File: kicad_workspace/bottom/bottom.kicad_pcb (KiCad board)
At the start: 2 copper layers, 76.8 x 84 mm, 28 parts, among them M1 N20_MOTOR_EXTENDED_SHAFT, M2 N20_MOTOR_EXTENDED_SHAFT, U1 DRV8833PWP, U2 ULTRASOUND_T_R, U3 ATmega4809-A, U4 BNO055, Y1 32.768kHz

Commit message: add battery connector
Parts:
- added J1: Battery connector, Connector_JST:JST_XH_B2B-XH-AM_1x02_P2.50mm_Vertical, F.Cu at (75.2, 89.9)
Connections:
- U1 pad 10: Net-(U1-BIN2) -> DRV_B2
- U1 pad 15: Net-(U1-AIN2) -> DRV_A2
- U1 pad 16: Net-(U1-AIN1) -> DRV_A1
- U1 pad 9: Net-(U1-BIN1) -> DRV_B1
- U3 pad 34: Net-(U1-BIN2) -> DRV_A1
- U3 pad 35: Net-(U1-BIN1) -> DRV_A2
- U3 pad 36: Net-(U1-AIN2) -> DRV_B1
- U3 pad 37: Net-(U1-AIN1) -> DRV_B2
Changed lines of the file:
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@@
   (net 13 "Net-(U1-BISEN)")
   (net 14 "unconnected-(U1-nFAULT-Pad8)")
-  (net 15 "Net-(U1-BIN1)")
-  (net 16 "Net-(U1-BIN2)")
+  (net 15 "VCC")
+  (net 16 "DRV_B1")
   (net 17 "Net-(U1-VCP)")
-  (net 18 "Net-(U1-AIN2)")
-  (net 19 "Net-(U1-AIN1)")
+  (net 18 "DRV_B2")
+  (net 19 "DRV_A2")
   (net 20 "Net-(U2-SIG)")
   (net 21 "Net-(JP1-C)")
@@
   (net 73 "unconnected-(U6-GPIO1-Pad5)")
   (net 74 "unconnected-(U7-GPIO1-Pad5)")
+  (net 75 "DRV_A1")
   (footprint "pololu:ULTRASOUND_T_R" (layer "F.Cu")
     (at 60.325 38.1)
@@
       (scale (xyz 1 1 1))
       (rotate (xyz 0 180 180))
+    )
+  )
+  (footprint "Connector_JST:JST_XH_B2B-XH-AM_1x02_P2.50mm_Vertical" (layer "F.Cu")
+    (at 75.224 89.916)
+    (descr "JST XH series connector, B2B-XH-AM, with boss (http://www.jst-mfg.com/product/pdf/eng/eXH.pdf), generated with kicad-footprint-generator")
+    (tags "connector JST XH vertical boss")
+    (property "Sheetfile" "bottom.kicad_sch")
+    (property "Sheetname" "")
+    (property "ki_description" "Generic connector, single row, 01x02, script generated (kicad-library-utils/schlib/autogen/connector/)")
+    (property "ki_keywords" "connector")
+    (attr through_hole)
+    (fp_text reference "J1" (at 1.25 -3.55) (layer "F.SilkS")
+        (effects (font (size 1 1) (thickness 0.15)))
+    )
+    (fp_text value "Battery connector" (at 1.25 4.6) (layer "F.Fab")
+        (effects (font (size 1 1) (thickness 0.15)))
+    )
+    (fp_text user "${REFERENCE}" (at 1.25 2.7) (layer "F.Fab")
+        (effects (font (size 1 1) (thickness 0.15)))
+    )
+    (fp_line (start -2.85 -2.75) (end -2.85 -1.5)
+      (stroke (width 0.12) (type solid)) (layer "F.SilkS"))
+    (fp_line (start -2.56 -2.46) (end -2.56 3.51)
+      (stroke (width 0.12) (type solid)) (layer "F.SilkS"))
+    (fp_line (start -2.56 3.51) (end 5.06 3.51)
+      (stroke (width 0.12) (type solid)) (layer "F.SilkS"))
+    (fp_line (start -2.55 -2.45) (end -2.55 -1.7)
+      (stroke (width 0.12) (type solid)) (layer "F.SilkS"))
+    (fp_line (start -2.55 -1.7) (end -0.75 -1.7)
+      (stroke (width 0.12) (type solid)) (layer "F.SilkS"))
+    (fp_line (start -2.55 -0.2) (end -1.8 -0.2)
+      (stroke (width 0.12) (type solid)) (layer "F.SilkS"))
+    (fp_line (start -1.8 -0.2) (end -1.8 1.14)
+      (stroke (width 0.12) (type solid)) (layer "F.SilkS"))
+    (fp_line (start -1.6 -2.75) (end -2.85 -2.75)
+      (stroke (width 0.12) (type solid)) (layer "F.SilkS"))
+    (fp_line (start -0.75 -2.45) (end -2.55 -2.45)
+      (stroke (width 0.12) (type solid)) (layer "F.SilkS"))
+    (fp_line (start -0.75 -1.7) (end -0.75 -2.45)
+      (stroke (width 0.12) (type solid)) (layer "F.SilkS"))
+    (fp_line (start 0.75 -2.45) (end 0.75 -1.7)
+      (stroke (width 0.12) (type solid)) (layer "F.SilkS"))
+    (fp_line (start 0.75 -1.7) (end 1.75 -1.7)
+      (stroke (width 0.12) (type solid)) (layer "F.SilkS"))
+    (fp_line (start 1.25 2.75) (end -0.74 2.75)
+      (stroke (width 0.12) (type solid)) (layer "F.SilkS"))
+    (fp_line (start 1.75 -2.45) (end 0.75 -2.45)
+      (stroke (width 0.12) (type solid)) (layer "F.SilkS"))
+    (fp_line (start 1.75 -1.7) (end 1.75 -2.45)
+      (stroke (width 0.12) (type solid)) (layer "F.SilkS"))
+    (fp_line (start 3.25 -2.45) (end 3.25 -1.7)
+      (stroke (width 0.12) (type solid)) (layer "F.SilkS"))
+    (fp_line (start 3.25 -1.7) (end 5.05 -1.7)
+      (stroke (width 0.12) (type solid)) (layer "F.SilkS"))
+    (fp_line (start 4.3 -0.2) (end 4.3 2.75)
+      (stroke (width 0.12) (type solid)) (layer "F.SilkS"))
+    (fp_line (start 4.3 2.75) (end 1.25 2.75)
+      (stroke (width 0.12) (type solid)) (layer "F.SilkS"))
+    (fp_line (start 5.05 -2.45) (end 3.25 -2.45)
+      (stroke (width 0.12) (type solid)) (layer "F.SilkS"))
+    (fp_line (start 5.05 -1.7) (end 5.05 -2.45)
+      (stroke (width 0.12) (type solid)) (layer "F.SilkS"))
+    (fp_line (start 5.05 -0.2) (end 4.3 -0.2)
+      (stroke (width 0.12) (type solid)) (layer "F.SilkS"))
+    (fp_line (start 5.06 -2.46) (end -2.56 -2.46)
+      (stroke (width 0.12) (type solid)) (layer "F.SilkS"))
+    (fp_line (start 5.06 3.51) (end 5.06 -2.46)
+      (stroke (width 0.12) (type solid)) (layer "F.SilkS"))
+    (fp_line (start -2.95 -2.85) (end -2.95 3.9)
+      (stroke (width 0.05) (type solid)) (layer "F.CrtYd"))
+    (fp_line (start -2.95 3.9) (end 5.45 3.9)
+      (stroke (width 0.05) (type solid)) (layer "F.CrtYd"))
+    (fp_line (start 5.45 -2.85) (end -2.95 -2.85)
+      (stroke (width 0.05) (type solid)) (layer "F.CrtYd"))
+    (fp_line (start 5.45 3.9) (end 5.45 -2.85)
+      (stroke (width 0.05) (type solid)) (layer "F.CrtYd"))
+    (fp_line (start -2.45 -2.35) (end -2.45 3.4)
+      (stroke (width 0.1) (type solid)) (layer "F.Fab"))
+    (fp_line (start -2.45 3.4) (end 4.95 3.4)
+      (stroke (width 0.1) (type solid)) (layer "F.Fab"))
+    (fp_line (start -0.625 -2.35) (end 0 -1.35)
+      (stroke (width 0.1) (type solid)) (layer "F.Fab"))
+    (fp_line (start 0 -1.35) (end 0.625 -2.35)
+      (stroke (width 0.1) (type solid)) (layer "F.Fab"))
+    (fp_line (start 4.95 -2.35) (end -2.45 -2.35)
+      (stroke (width 0.1) (type solid)) (layer "F.Fab"))
+    (fp_line (start 4.95 3.4) (end 4.95 -2.35)
+      (stroke (width 0.1) (type solid)) (layer "F.Fab"))
+    (pad "" np_thru_hole circle (at -1.6 2) (size 1.2 1.2) (drill 1.2) (layers "*.Cu" "*.Mask"))
+    (pad "1" thru_hole roundrect (at 0 0) (size 1.7 2) (drill 1) (layers "*.Cu" "*.Mask") (roundrect_rratio 0.147059)
+      (net 15 "VCC") (pinfunction "Pin_1") (pintype "passive"))
+    (pad "2" thru_hole oval (at 2.5 0) (size 1.7 2) (drill 1) (layers "*.Cu" "*.Mask")
+      (net 1 "GND") (pinfunction "Pin_2") (pintype "passive"))
+    (model "${KICAD7_3DMODEL_DIR}/Connector_JST.3dshapes/JST_XH_B2B-XH-A_1x02_P2.50mm_Vertical.step"
+      (offset (xyz 0 0 0))
+      (scale (xyz 1 1 1))
+      (rotate (xyz 0 0 0))
     )
   )
@@
     (fp_arc (start -4.277996 -4.277996) (mid -5.350166 -3.264983) (end -6.75 -2.8)
       (stroke (width 0.12) (type solid)) (layer "B.SilkS"))
-    (fp_arc (start 4.277996 4.277996) (mid 5.350166 3.264983) (end 6.75 2.8)
+    (fp_arc (start 4.277996 4.277996) (mid 5.350166 3.264984) (end 6.75 2.8)
       (stroke (width 0.12) (type solid)) (layer "B.SilkS"))
     (fp_arc (start 5.988332 0.861605) (mid 0 6.049999) (end -5.988332 0.861605)
       (stroke (width 0.12) (type solid)) (layer "B.SilkS"))
-    (fp_arc (start 6.75 -2.8) (mid 5.350172 -3.264989) (end 4.277997 -4.277996)
+    (fp_arc (start 6.75 -2.8) (mid 5.350172 -3.264991) (end 4.277997 -4.277996)
       (stroke (width 0.12) (type solid)) (layer "B.SilkS"))
     (fp_arc (start 6.75 -2.8) (mid 9.55 0) (end 6.75 2.8)
@@
       (net 14 "unconnected-(U1-nFAULT-Pad8)") (pinfunction "nFAULT") (pintype "open_collector+no_connect"))
     (pad "9" smd roundrect (at 2.8625 -2.275 180) (size 1.575 0.4) (layers "B.Cu" "B.Paste" "B.Mask") (roundrect_rratio 0.25)
-      (net 15 "Net-(U1-BIN1)") (pinfunction "BIN1") (pintype "input"))
+      (net 16 "DRV_B1") (pinfunction "BIN1") (pintype "input"))
     (pad "10" smd roundrect (at 2.8625 -1.625 180) (size 1.575 0.4) (layers "B.Cu" "B.Paste" "B.Mask") (roundrect_rratio 0.25)
-      (net 16 "Net-(U1-BIN2)") (pinfunction "BIN2") (pintype "input"))
+      (net 18 "DRV_B2") (pinfunction "BIN2") (pintype "input"))
     (pad "11" smd roundrect (at 2.8625 -0.975 180) (size 1.575 0.4) (layers "B.Cu" "B.Paste" "B.Mask") (roundrect_rratio 0.25)
       (net 17 "Net-(U1-VCP)") (pinfunction "VCP") (pintype "bidirectional"))
@@
       (net 22 "+3.3V") (pinfunction "VINT") (pintype "power_in"))
     (pad "15" smd roundrect (at 2.8625 1.625 180) (size 1.575 0.4) (layers "B.Cu" "B.Paste" "B.Mask") (roundrect_rratio 0.25)
-      (net 18 "Net-(U1-AIN2)") (pinfunction "AIN2") (pintype "input"))
+      (net 19 "DRV_A2") (pinfunction "AIN2") (pintype "input"))
     (pad "16" smd roundrect (at 2.8625 2.275 180) (size 1.575 0.4) (layers "B.Cu" "B.Paste" "B.Mask") (roundrect_rratio 0.25)
-      (net 19 "Net-(U1-AIN1)") (pinfunction "AIN1") (pintype "input"))
+      (net 75 "DRV_A1") (pinfunction "AIN1") (pintype "input"))
     (pad "17" thru_hole circle (at -0.75 -1.5 180) (size 0.5 0.5) (drill 0.2) (layers "*.Cu")
       (net 1 "GND") (pinfunction "GND(PPAD)") (pintype "power_in"))
@@
       (net 47 "unconnected-(U3-PE3-Pad33)") (pinfunction "PE3") (pintype "bidirectional+no_connect"))
     (pad "34" smd roundrect (at 4.1625 1.75 180) (size 1.475 0.3) (layers "B.Cu" "B.Paste" "B.Mask") (roundrect_rratio 0.25)
-      (net 16 "Net-(U1-BIN2)") (pinfunction "PF0") (pintype "bidirectional"))
+      (net 75 "DRV_A1") (pinfunction "PF0") (pintype "bidirectional"))
     (pad "35" smd roundrect (at 4.1625 2.25 180) (size 1.475 0.3) (layers "B.Cu" "B.Paste" "B.Mask") (roundrect_rratio 0.25)
-      (net 15 "Net-(U1-BIN1)") (pinfunction "PF1") (pintype "bidirectional"))
+      (net 19 "DRV_A2") (pinfunction "PF1") (pintype "bidirectional"))
     (pad "36" smd roundrect (at 4.1625 2.75 180) (size 1.475 0.3) (layers "B.Cu" "B.Paste" "B.Mask") (roundrect_rratio 0.25)
-      (net 18 "Net-(U1-AIN2)") (pinfunction "PF2") (pintype "bidirectional"))
+      (net 16 "DRV_B1") (pinfunction "PF2") (pintype "bidirectional"))
     (pad "37" smd roundrect (at 2.75 4.1625 180) (size 0.3 1.475) (layers "B.Cu" "B.Paste" "B.Mask") (roundrect_rratio 0.25)
-      (net 19 "Net-(U1-AIN1)") (pinfunction "PF3") (pintype "bidirectional"))
+      (net 18 "DRV_B2") (pinfunction "PF3") (pintype "bidirectional"))
     (pad "38" smd roundrect (at 2.25 4.1625 180) (size 0.3 1.475) (layers "B.Cu" "B.Paste" "B.Mask") (roundrect_rratio 0.25)
       (net 48 "unconnected-(U3-PF4-Pad38)") (pinfunction "PF4") (pintype "bidirectional+no_connect"))

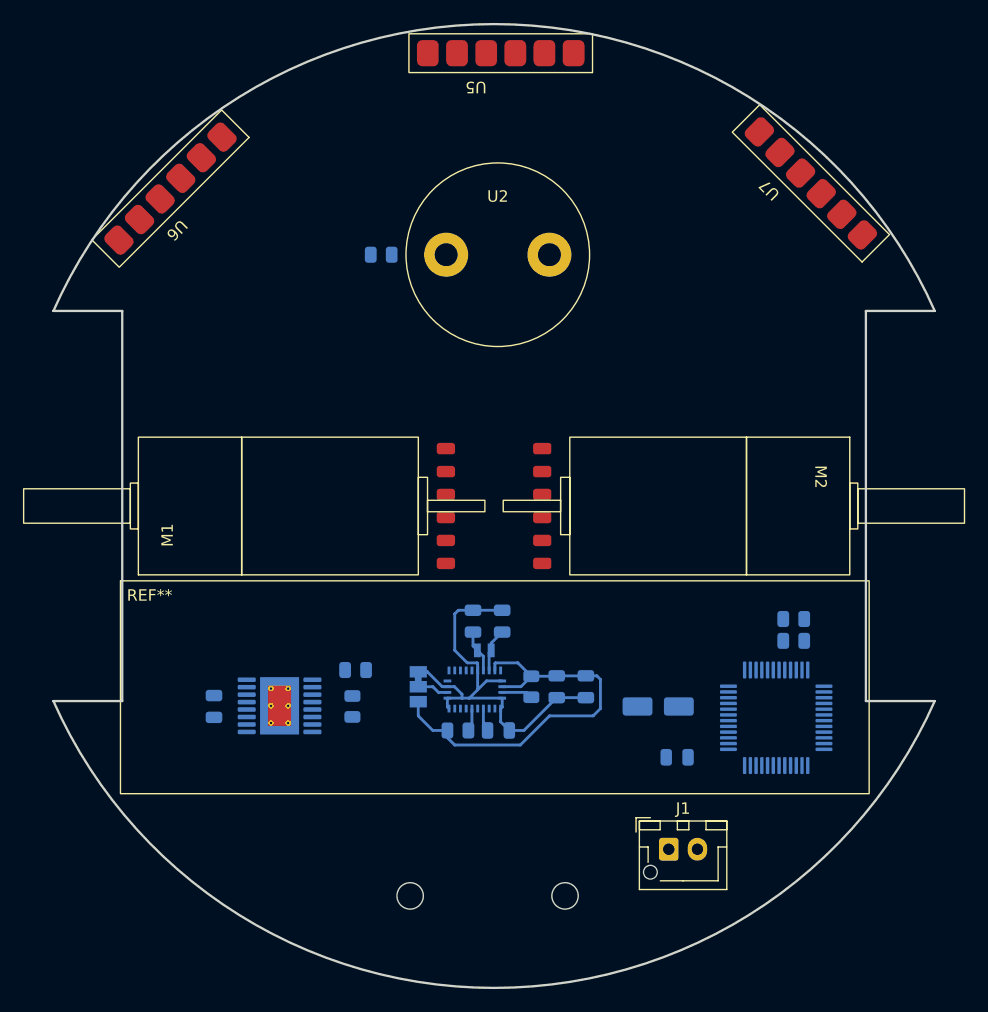
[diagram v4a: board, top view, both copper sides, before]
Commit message: add dw01 and its mosfets to schematic and pcb
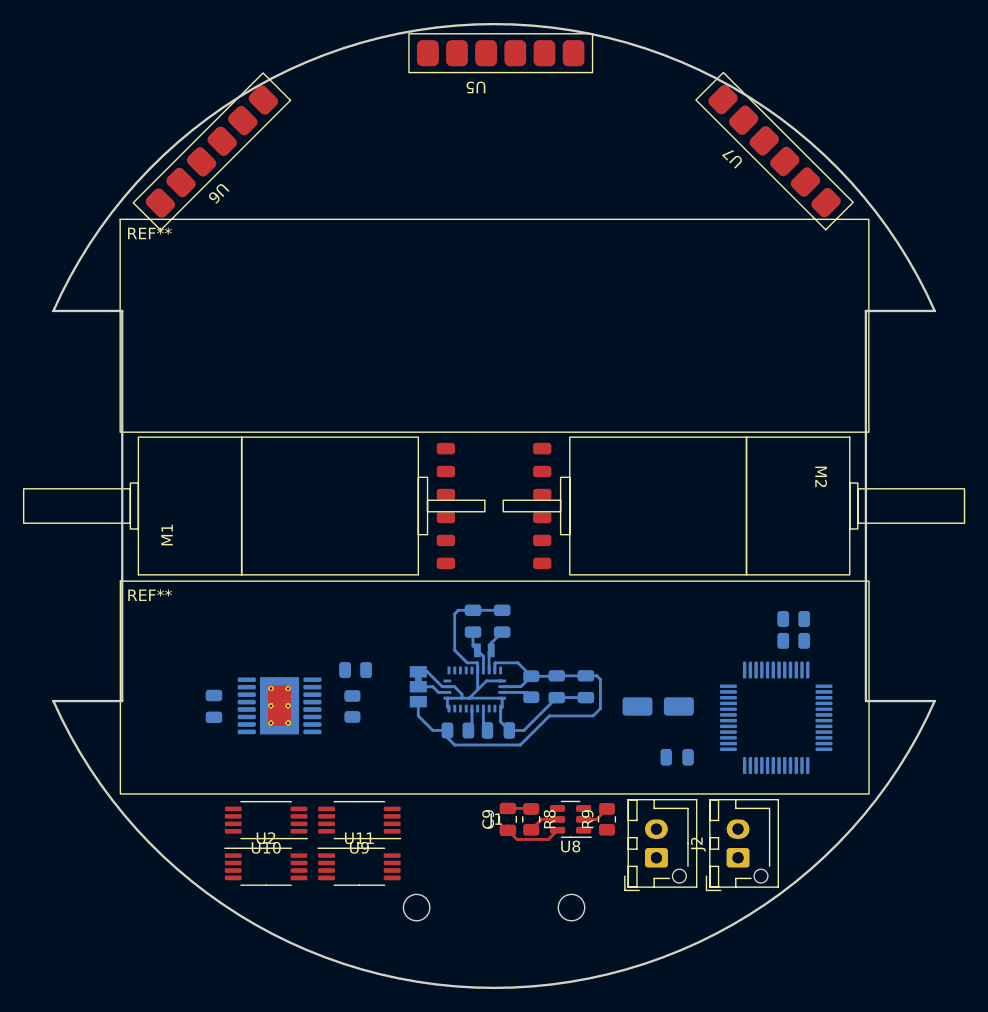
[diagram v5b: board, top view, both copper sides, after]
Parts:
- removed R3: R, Resistor_SMD:R_0805_2012Metric
- removed the REF** at (27.4, 66.5)
- added C9: 100nF, Capacitor_SMD:C_0805_2012Metric, F.Cu at (61.2, 87.3)
- added J2: Battery connector, Connector_JST:JST_XH_B2B-XH-AM_1x02_P2.50mm_Vertical, F.Cu at (81.3, 90.7)
- added R8: 100R, Resistor_SMD:R_0805_2012Metric, F.Cu at (63.2, 87.3)
- added R9: 1K, Resistor_SMD:R_0805_2012Metric, F.Cu at (69.8, 87.3)
- added REF**: SAMSUNG_18650, pololu:SAMSUNG_18650, F.Cu at (27.4, 66.5)
- added REF**: SAMSUNG_18650, pololu:SAMSUNG_18650, F.Cu at (27.4, 35.0)
- added U10: ~, Package_SO:TSSOP-8_4.4x3mm_P0.65mm, F.Cu at (40.1, 87.4)
- added U11: ~, Package_SO:TSSOP-8_4.4x3mm_P0.65mm, F.Cu at (48.3, 91.4)
- added U8: ~, Package_TO_SOT_SMD:SOT-23-6, F.Cu at (66.7, 87.3)
- added U9: ~, Package_SO:TSSOP-8_4.4x3mm_P0.65mm, F.Cu at (48.3, 87.4)
- U2: value ULTRASOUND_T_R -> ~; footprint pololu:ULTRASOUND_T_R -> Package_SO:TSSOP-8_4.4x3mm_P0.65mm
- moved U2 57.0 mm to (40.1, 91.4)
- moved U6 4.84 mm to (42.3, 24.6)
- moved U7 4.23 mm to (88.9, 35.9)
- moved J1 1.30 mm to (74.2, 90.7), turned to 90 degrees
- moved REF** 1.17 mm to (60.0, 95.0)
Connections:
- J1 pad 1: VCC -> +BATT
- J1 pad 2: GND -> -BATT
- U2 pad 1: GND -> Net-(U2-D-Pad1)
- U2 pad 2: Net-(U2-SIG) -> -BATT
- U3 pad 48: Net-(U3-PA4) -> unconnected-(U3-PA4-Pad48)
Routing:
- net -BATT: track 0.00 -> 5.35 mm
- net Net-(U8-VCC): track 0.00 -> 2.67 mm
- net Net-(U8-CS): track 0.00 -> 2.41 mm
- net +BATT: track 0.00 -> 2.05 mm

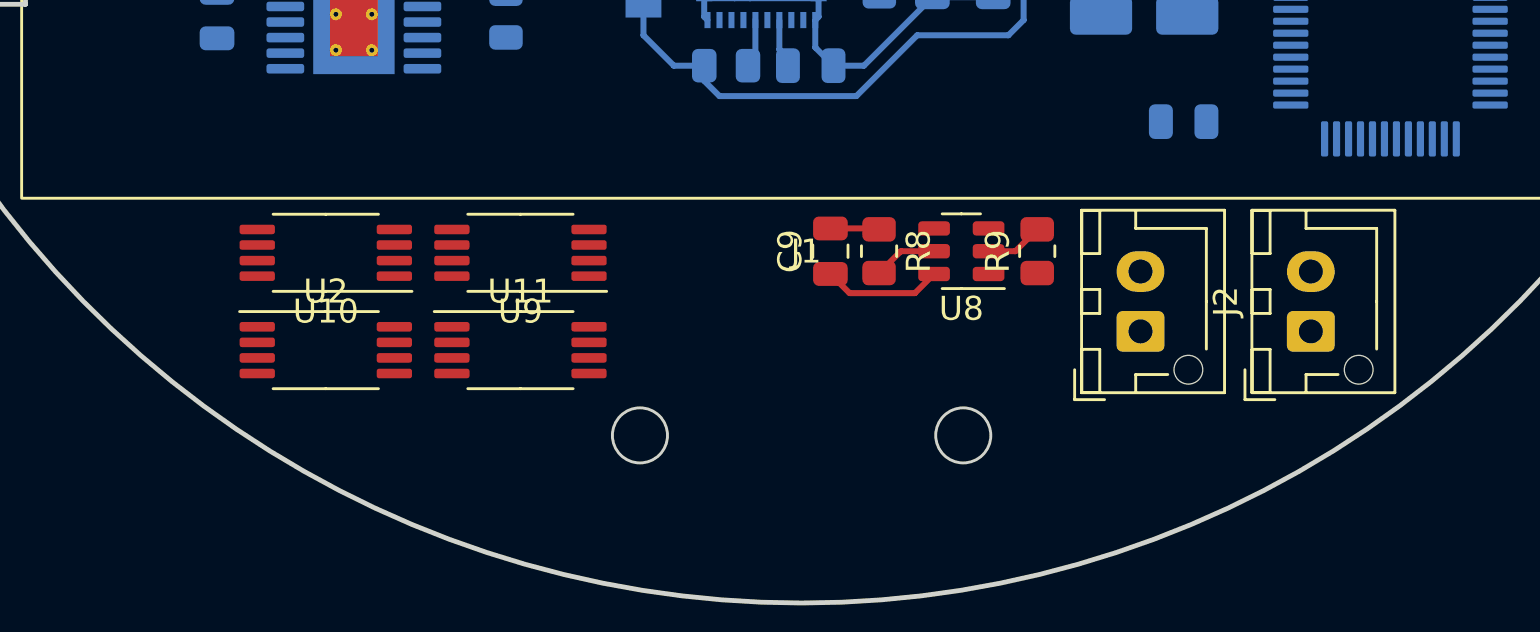
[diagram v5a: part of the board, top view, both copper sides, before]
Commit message: wired dw01 and 4x 8205a mosfets
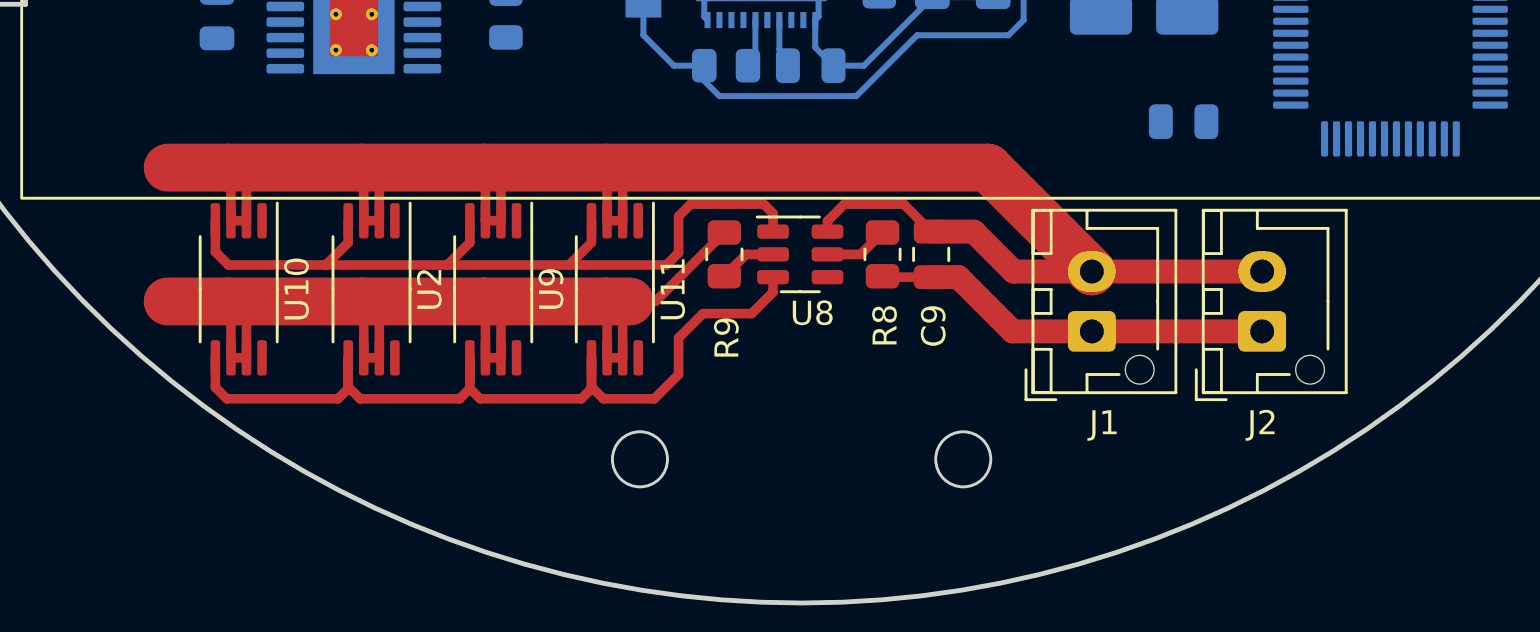
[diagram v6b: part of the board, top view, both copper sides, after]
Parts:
- moved R9 13.1 mm to (56.8, 87.4), turned to -90 degrees
- moved U8 6.73 mm to (59.9, 87.4), turned to 0 degrees
- moved U11 4.69 mm to (52.2, 88.9), turned to -90 degrees
- moved C9 4.21 mm to (65.4, 87.4), turned to -90 degrees
- moved U10 3.94 mm to (36.5, 88.9), turned to -90 degrees
- moved U2 3.18 mm to (42.0, 88.9), turned to -90 degrees
- moved J2 2.03 mm to (79.2, 90.7)
- moved J1 2.03 mm to (72.1, 90.7)
- moved U9 1.90 mm to (47.1, 88.9), turned to -90 degrees
- moved REF** 1.00 mm to (60.0, 96.0)
- moved R8 0.19 mm to (63.4, 87.4), turned to 90 degrees
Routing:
- net -BATT: track 5.35 -> 82.5 mm
- net Net-(R9-Pad1): track 0.00 -> 47.2 mm
- net Net-(U10-G2): track 0.00 -> 36.4 mm
- net Net-(U10-G1): track 0.00 -> 34.4 mm
- net +BATT: track 2.05 -> 16.8 mm
